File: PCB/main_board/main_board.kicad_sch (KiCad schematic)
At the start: 55 parts, among them CN1 XT30PW-M, CN2 XT30PW-M, U1 XT30PW-F, U2 W25Q32JVUUIQ, U3 W25N01GVZEIG_C907680, U4 INA226, U5 INA226, U6 RP2040, U7 AZ1117-3.3, X1 X322512MSB4SI

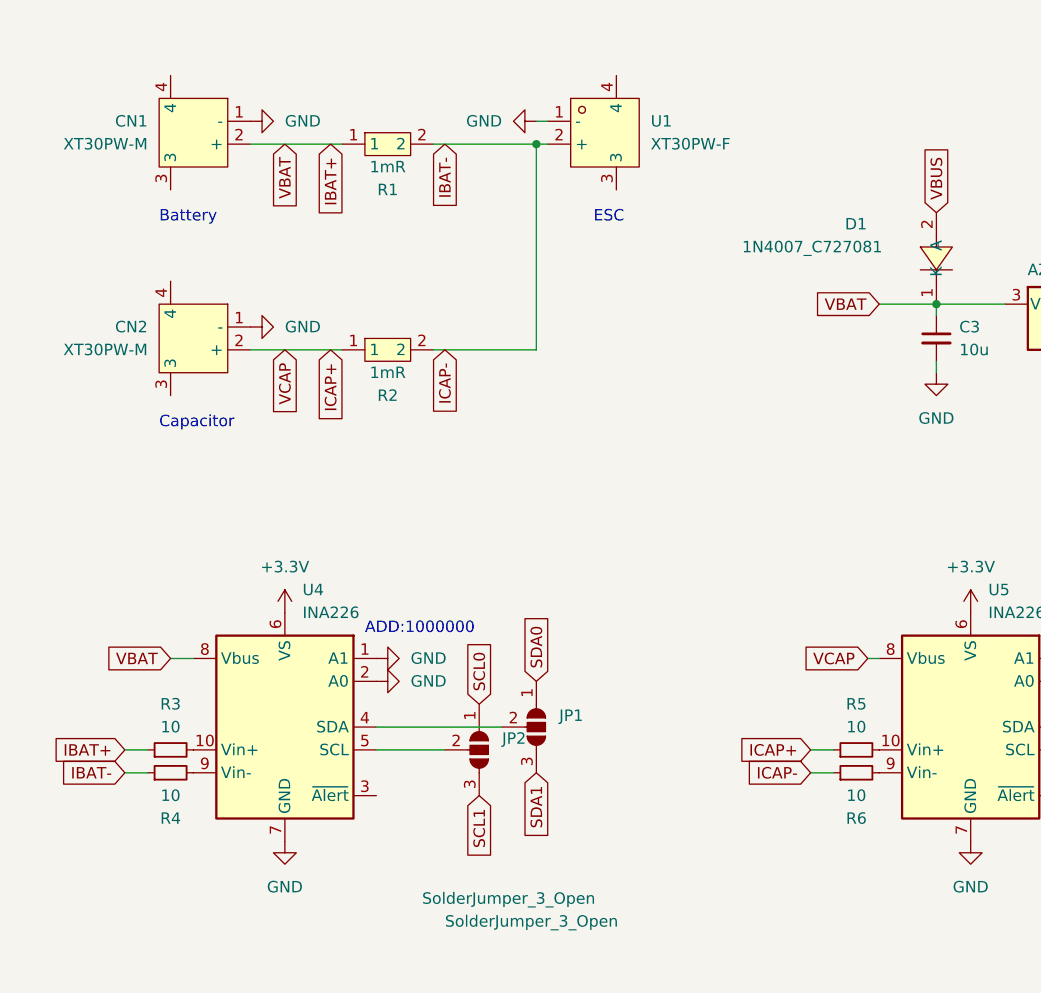
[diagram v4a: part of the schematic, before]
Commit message: Complete high current trace
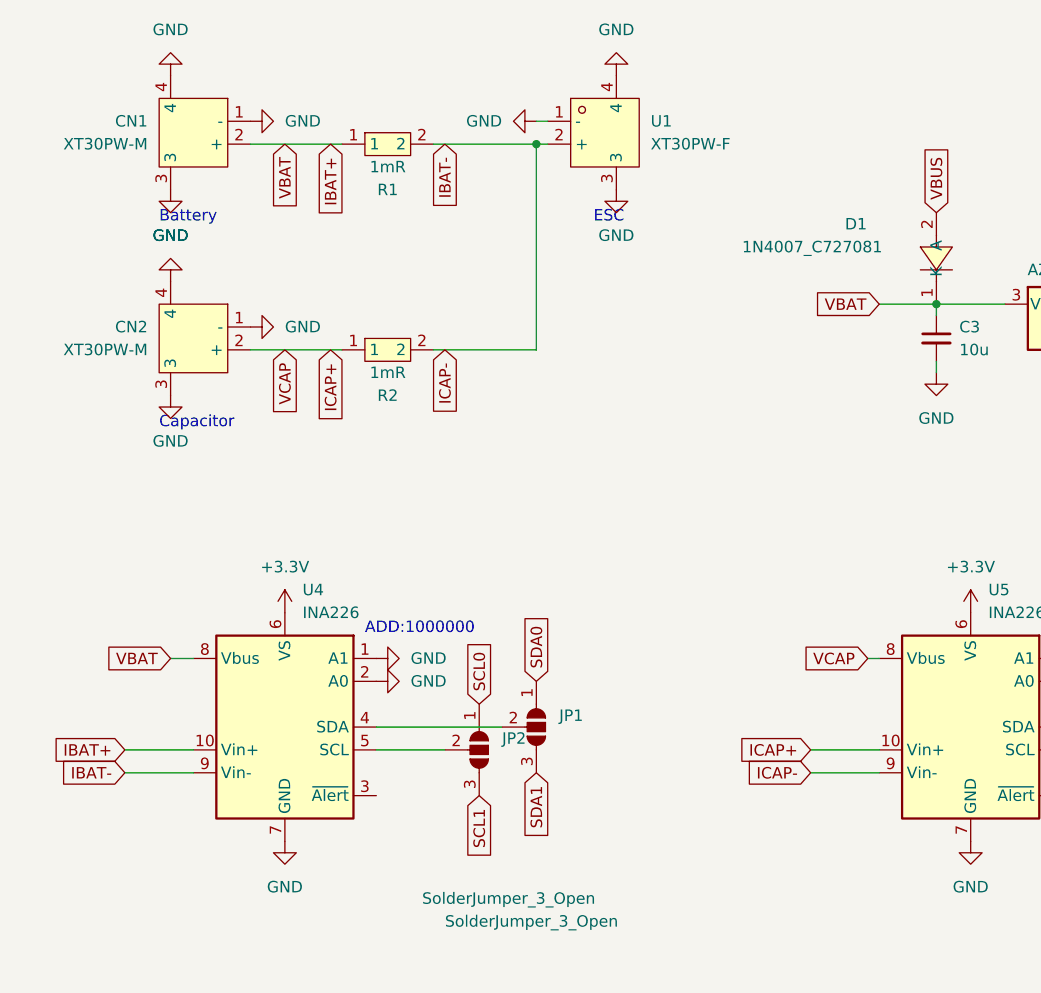
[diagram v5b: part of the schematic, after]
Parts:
- removed R3, R4, R5, R6: 10, Resistor_SMD:R_0402_1005Metric, symbol Device:R_Small
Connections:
- net GND: now also CN1.3, CN1.4, CN2.3, CN2.4, U1.3, U1.4
- net IBAT+: now also U4.10 (Vin+)
- net IBAT-: now also U4.9 (Vin-), U5.9 (Vin-)
- net ICAP+: now also U5.10 (Vin+)
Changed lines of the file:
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@@
     (stroke (width 0) (type default))
   )
-  (wire (pts (xy 123.19 110.49) (xy 125.73 110.49))
+  (wire (pts (xy 123.19 110.49) (xy 130.81 110.49))
     (stroke (width 0) (type default))
   )
@@
     (stroke (width 0) (type default))
   )
-  (wire (pts (xy 46.99 110.49) (xy 49.53 110.49))
+  (wire (pts (xy 46.99 110.49) (xy 54.61 110.49))
     (stroke (width 0) (type default))
   )
@@
     (stroke (width 0) (type default))
   )
-  (wire (pts (xy 123.19 107.95) (xy 125.73 107.95))
+  (wire (pts (xy 123.19 107.95) (xy 130.81 107.95))
     (stroke (width 0) (type default))
   )
@@
     (stroke (width 0) (type default))
   )
-  (wire (pts (xy 46.99 107.95) (xy 49.53 107.95))
+  (wire (pts (xy 46.99 107.95) (xy 54.61 107.95))
     (stroke (width 0) (type default))
   )
@@
     )
   )
+  (symbol (lib_id "power:GND") (at 52.07 68.58 0) (unit 1)
+    (in_bom yes) (on_board yes) (dnp no) (fields_autoplaced)
+    (property "Reference" "#PWR048" (at 52.07 74.93 0)
+      (effects (font (size 1.27 1.27)) hide)
+    )
+    (property "Value" "GND" (at 52.07 73.66 0)
+      (effects (font (size 1.27 1.27)))
+    )
+    (property "Footprint" "" (at 52.07 68.58 0)
+      (effects (font (size 1.27 1.27)) hide)
+    )
+    (property "Datasheet" "" (at 52.07 68.58 0)
+      (effects (font (size 1.27 1.27)) hide)
+    )
+    (pin "1")
+    (instances
+      (project "main_board"
+        (path "/fd1b5ed6-edd1-4f0a-921b-555919c14d96"
+          (reference "#PWR048") (unit 1)
+        )
+      )
+    )
+  )
   (symbol (lib_id "power:GND") (at 254 196.85 180) (unit 1)
     (in_bom yes) (on_board yes) (dnp no) (fields_autoplaced)
@@
     )
   )
-  (symbol (lib_id "Device:R_Small") (at 52.07 110.49 90) (unit 1)
-    (in_bom yes) (on_board yes) (dnp no)
-    (property "Reference" "R4" (at 52.07 115.57 90)
-      (effects (font (size 1.27 1.27)))
-    )
-    (property "Value" "10" (at 52.07 113.03 90)
-      (effects (font (size 1.27 1.27)))
-    )
-    (property "Footprint" "Resistor_SMD:R_0402_1005Metric" (at 52.07 110.49 0)
-      (effects (font (size 1.27 1.27)) hide)
-    )
-    (property "Datasheet" "~" (at 52.07 110.49 0)
-      (effects (font (size 1.27 1.27)) hide)
-    )
-    (pin "1")
-    (pin "2")
-    (instances
-      (project "main_board"
-        (path "/fd1b5ed6-edd1-4f0a-921b-555919c14d96"
-          (reference "R4") (unit 1)
+  (symbol (lib_id "power:GND") (at 101.6 45.72 0) (unit 1)
+    (in_bom yes) (on_board yes) (dnp no) (fields_autoplaced)
+    (property "Reference" "#PWR049" (at 101.6 52.07 0)
+      (effects (font (size 1.27 1.27)) hide)
+    )
+    (property "Value" "GND" (at 101.6 50.8 0)
+      (effects (font (size 1.27 1.27)))
+    )
+    (property "Footprint" "" (at 101.6 45.72 0)
+      (effects (font (size 1.27 1.27)) hide)
+    )
+    (property "Datasheet" "" (at 101.6 45.72 0)
+      (effects (font (size 1.27 1.27)) hide)
+    )
+    (pin "1")
+    (instances
+      (project "main_board"
+        (path "/fd1b5ed6-edd1-4f0a-921b-555919c14d96"
+          (reference "#PWR049") (unit 1)
+        )
+      )
+    )
+  )
+  (symbol (lib_id "power:GND") (at 52.07 45.72 0) (unit 1)
+    (in_bom yes) (on_board yes) (dnp no) (fields_autoplaced)
+    (property "Reference" "#PWR047" (at 52.07 52.07 0)
+      (effects (font (size 1.27 1.27)) hide)
+    )
+    (property "Value" "GND" (at 52.07 50.8 0)
+      (effects (font (size 1.27 1.27)))
+    )
+    (property "Footprint" "" (at 52.07 45.72 0)
+      (effects (font (size 1.27 1.27)) hide)
+    )
+    (property "Datasheet" "" (at 52.07 45.72 0)
+      (effects (font (size 1.27 1.27)) hide)
+    )
+    (pin "1")
+    (instances
+      (project "main_board"
+        (path "/fd1b5ed6-edd1-4f0a-921b-555919c14d96"
+          (reference "#PWR047") (unit 1)
         )
       )
@@
     )
   )
-  (symbol (lib_id "Device:R_Small") (at 52.07 107.95 90) (unit 1)
-    (in_bom yes) (on_board yes) (dnp no) (fields_autoplaced)
-    (property "Reference" "R3" (at 52.07 102.87 90)
-      (effects (font (size 1.27 1.27)))
-    )
-    (property "Value" "10" (at 52.07 105.41 90)
-      (effects (font (size 1.27 1.27)))
-    )
-    (property "Footprint" "Resistor_SMD:R_0402_1005Metric" (at 52.07 107.95 0)
-      (effects (font (size 1.27 1.27)) hide)
-    )
-    (property "Datasheet" "~" (at 52.07 107.95 0)
-      (effects (font (size 1.27 1.27)) hide)
-    )
-    (pin "1")
-    (pin "2")
-    (instances
-      (project "main_board"
-        (path "/fd1b5ed6-edd1-4f0a-921b-555919c14d96"
-          (reference "R3") (unit 1)
+  (symbol (lib_id "power:GND") (at 52.07 55.88 180) (unit 1)
+    (in_bom yes) (on_board yes) (dnp no) (fields_autoplaced)
+    (property "Reference" "#PWR050" (at 52.07 49.53 0)
+      (effects (font (size 1.27 1.27)) hide)
+    )
+    (property "Value" "GND" (at 52.07 50.8 0)
+      (effects (font (size 1.27 1.27)))
+    )
+    (property "Footprint" "" (at 52.07 55.88 0)
+      (effects (font (size 1.27 1.27)) hide)
+    )
+    (property "Datasheet" "" (at 52.07 55.88 0)
+      (effects (font (size 1.27 1.27)) hide)
+    )
+    (pin "1")
+    (instances
+      (project "main_board"
+        (path "/fd1b5ed6-edd1-4f0a-921b-555919c14d96"
+          (reference "#PWR050") (unit 1)
         )
       )
@@
     )
   )
-  (symbol (lib_id "Device:R_Small") (at 128.27 107.95 90) (unit 1)
-    (in_bom yes) (on_board yes) (dnp no) (fields_autoplaced)
-    (property "Reference" "R5" (at 128.27 102.87 90)
-      (effects (font (size 1.27 1.27)))
-    )
-    (property "Value" "10" (at 128.27 105.41 90)
-      (effects (font (size 1.27 1.27)))
-    )
-    (property "Footprint" "Resistor_SMD:R_0402_1005Metric" (at 128.27 107.95 0)
-      (effects (font (size 1.27 1.27)) hide)
-    )
-    (property "Datasheet" "~" (at 128.27 107.95 0)
-      (effects (font (size 1.27 1.27)) hide)
-    )
-    (pin "1")
-    (pin "2")
-    (instances
-      (project "main_board"
-        (path "/fd1b5ed6-edd1-4f0a-921b-555919c14d96"
-          (reference "R5") (unit 1)
-        )
-      )
-    )
-  )
   (symbol (lib_id "Sensor_Energy:INA226") (at 64.77 105.41 0) (unit 1)
     (in_bom yes) (on_board yes) (dnp no) (fields_autoplaced)
@@
     )
   )
-  (symbol (lib_id "Device:R_Small") (at 128.27 110.49 90) (unit 1)
-    (in_bom yes) (on_board yes) (dnp no)
-    (property "Reference" "R6" (at 128.27 115.57 90)
-      (effects (font (size 1.27 1.27)))
-    )
-    (property "Value" "10" (at 128.27 113.03 90)
-      (effects (font (size 1.27 1.27)))
-    )
-    (property "Footprint" "Resistor_SMD:R_0402_1005Metric" (at 128.27 110.49 0)
-      (effects (font (size 1.27 1.27)) hide)
-    )
-    (property "Datasheet" "~" (at 128.27 110.49 0)
-      (effects (font (size 1.27 1.27)) hide)
-    )
-    (pin "1")
-    (pin "2")
-    (instances
-      (project "main_board"
-        (path "/fd1b5ed6-edd1-4f0a-921b-555919c14d96"
-          (reference "R6") (unit 1)
-        )
-      )
-    )
-  )
   (symbol (lib_id "power:+3.3V") (at 207.01 180.34 90) (unit 1)
     (in_bom yes) (on_board yes) (dnp no) (fields_autoplaced)
@@
     )
   )
+  (symbol (lib_id "power:GND") (at 52.07 33.02 180) (unit 1)
+    (in_bom yes) (on_board yes) (dnp no) (fields_autoplaced)
+    (property "Reference" "#PWR051" (at 52.07 26.67 0)
+      (effects (font (size 1.27 1.27)) hide)
+    )
+    (property "Value" "GND" (at 52.07 27.94 0)
+      (effects (font (size 1.27 1.27)))
+    )
+    (property "Footprint" "" (at 52.07 33.02 0)
+      (effects (font (size 1.27 1.27)) hide)
+    )
+    (property "Datasheet" "" (at 52.07 33.02 0)
+      (effects (font (size 1.27 1.27)) hide)
+    )
+    (pin "1")
+    (instances
+      (project "main_board"
+        (path "/fd1b5ed6-edd1-4f0a-921b-555919c14d96"
+          (reference "#PWR051") (unit 1)
+        )
+      )
+    )
+  )
   (symbol (lib_id "Device:C_Small") (at 128.27 161.29 90) (unit 1)
     (in_bom yes) (on_board yes) (dnp no)
@@
         )
       )
+    )
+  )
+  (symbol (lib_id "power:GND") (at 101.6 33.02 180) (unit 1)
+    (in_bom yes) (on_board yes) (dnp no) (fields_autoplaced)
+    (property "Reference" "#PWR052" (at 101.6 26.67 0)
+      (effects (font (size 1.27 1.27)) hide)
+    )
+    (property "Value" "GND" (at 101.6 27.94 0)
+      (effects (font (size 1.27 1.27)))
+    )
+    (property "Footprint" "" (at 101.6 33.02 0)
+      (effects (font (size 1.27 1.27)) hide)
+    )
+    (property "Datasheet" "" (at 101.6 33.02 0)
+      (effects (font (size 1.27 1.27)) hide)
+    )
+    (pin "1")
+    (instances
+      (project "main_board"
+        (path "/fd1b5ed6-edd1-4f0a-921b-555919c14d96"
+          (reference "#PWR052") (unit 1)
+        )
+      )

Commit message: Complete USB DP routing
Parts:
- added TP1: SWCLK, TestPoint:TestPoint_Pad_1.5x1.5mm, symbol Connector:TestPoint
- added TP2: SWD, TestPoint:TestPoint_Pad_1.5x1.5mm, symbol Connector:TestPoint
- added TP3: UART0 TX, TestPoint:TestPoint_Pad_1.5x1.5mm, symbol Connector:TestPoint
- added TP4: UART0 RX, TestPoint:TestPoint_Pad_1.5x1.5mm, symbol Connector:TestPoint
- added TP5, TP6: GND, TestPoint:TestPoint_Pad_1.5x1.5mm, symbol Connector:TestPoint
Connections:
- net GND: now also Card1.10 (EP), Card1.11 (EP), Card1.12 (EP), Card1.13 (EP), U3.9 (EP), USB1.13 (SHELL), USB1.14 (SHELL), TP5.1, TP6.1
- net USB+: now reaches R17.1, USB1.7 (DN1)
- net USB-: now reaches R16.1, USB1.6 (DP1)
- net at U6.24 (SWCLK): now also TP1.1
- net at U6.25 (SWD): now also TP2.1
- net TX0: now reaches U6.28 (GPIO17)
- net TX0: now also TP3.1
- net RX0: now reaches U6.29 (GPIO18)
- net RX0: now also TP4.1

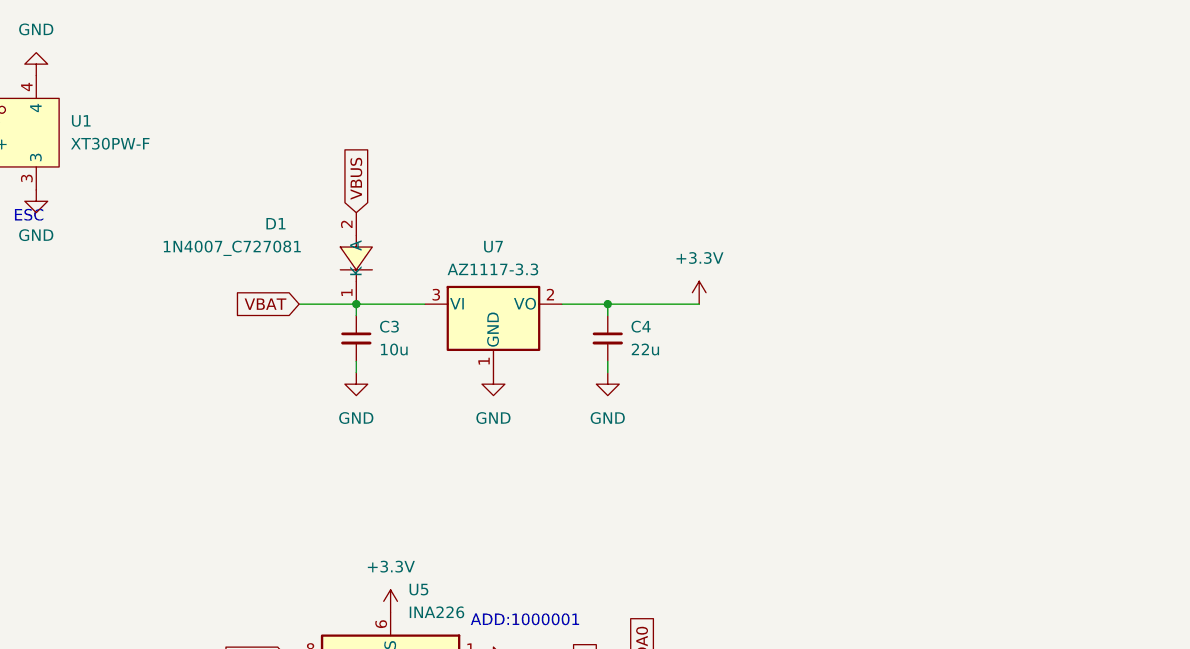
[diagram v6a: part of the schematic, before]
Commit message: Change LDO to BUCK converter
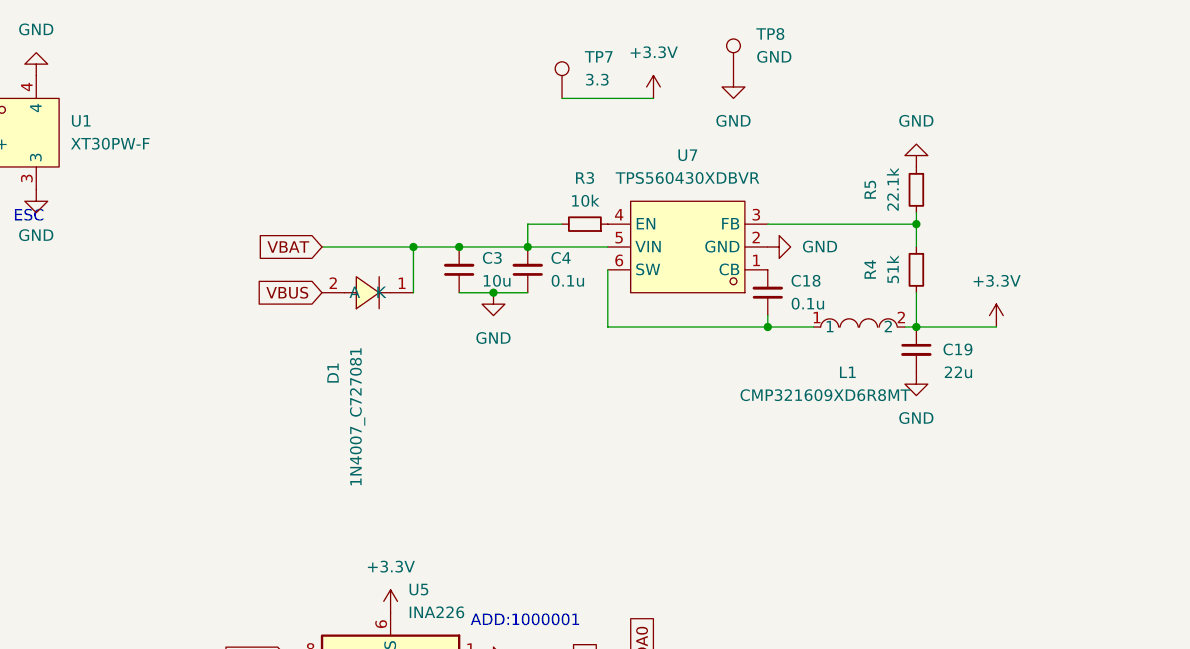
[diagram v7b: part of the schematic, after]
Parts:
- removed U7: AZ1117-3.3, Package_TO_SOT_SMD:SOT-89-3, symbol Regulator_Linear:AZ1117-3.3
- added C18: 0.1u, Capacitor_SMD:C_0402_1005Metric, symbol Device:C_Small
- added C19: 22u, Capacitor_SMD:C_0805_2012Metric, symbol Device:C_Small
- added L1: CMP321609XD6R8MT, pcb_lib:L1206, symbol pcb_lib:CMP321609XD6R8MT
- added R3: 10k, Capacitor_SMD:C_0402_1005Metric, symbol Device:R_Small
- added R4: 51k, Capacitor_SMD:C_0402_1005Metric, symbol Device:R_Small
- added R5: 22.1k, Capacitor_SMD:C_0402_1005Metric, symbol Device:R_Small
- added TP7: 3.3, TestPoint:TestPoint_Pad_1.5x1.5mm, symbol Connector:TestPoint
- added TP8: GND, TestPoint:TestPoint_Pad_1.5x1.5mm, symbol Connector:TestPoint
- added U7: TPS560430XDBVR, pcb_lib:SOT-23-6_L2.9-W1.6-P0.95-LS2.8-BL, symbol pcb_lib:TPS560430XDBVR
- C4: value 22u -> 0.1u
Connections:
- net +3.3V: now also C19.1, L1.2, R4.2, TP7.1; no longer C4.1
- net GND: now also C3.1, C4.1, C19.2, R5.1, TP8.1, U7.2 (GND); no longer C3.2, C4.2
- net IBAT+: now also C3.2, C4.2, R3.2, U7.5 (VIN); no longer C3.1
- new net: R4.1, R5.2, U7.3 (FB)
- new net: C18.1, L1.1, U7.6 (SW)
- new net: C18.2, U7.1 (CB)
- new net: R3.1, U7.4 (EN)
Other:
- moved on the sheet: D1

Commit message: Change INA226 package for SMT
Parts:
- C3, C4: footprint Capacitor_SMD:C_0402_1005Metric -> Capacitor_SMD:C_0603_1608Metric
- U4, U5: footprint Package_SO:VSSOP-10_3x3mm_P0.5mm -> pcb_lib:MSOP-10_L3.0-W3.0-P0.50-LS5.0-BL
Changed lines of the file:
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@@
       (effects (font (size 1.27 1.27)) (justify left))
     )
-    (property "Footprint" "Package_SO:VSSOP-10_3x3mm_P0.5mm" (at 161.29 116.84 0)
+    (property "Footprint" "pcb_lib:MSOP-10_L3.0-W3.0-P0.50-LS5.0-BL" (at 161.29 116.84 0)
       (effects (font (size 1.27 1.27)) hide)
     )
@@
       (effects (font (size 1.27 1.27)) (justify left))
     )
-    (property "Footprint" "Package_SO:VSSOP-10_3x3mm_P0.5mm" (at 85.09 116.84 0)
+    (property "Footprint" "pcb_lib:MSOP-10_L3.0-W3.0-P0.50-LS5.0-BL" (at 85.09 116.84 0)
       (effects (font (size 1.27 1.27)) hide)
     )
@@
       (effects (font (size 1.27 1.27)) (justify right))
     )
-    (property "Footprint" "Capacitor_SMD:C_0402_1005Metric" (at 148.59 54.61 0)
+    (property "Footprint" "Capacitor_SMD:C_0603_1608Metric" (at 148.59 54.61 0)
       (effects (font (size 1.27 1.27)) hide)
     )
@@
       (effects (font (size 1.27 1.27)) (justify right))
     )
-    (property "Footprint" "Capacitor_SMD:C_0402_1005Metric" (at 156.21 54.61 0)
-      (effects (font (size 1.27 1.27)) hide)
-    )
+    (property "Footprint" "Capacitor_SMD:C_0603_1608Metric" (at 156.21 54.61 0)
+      (effects (font (size 1.27 1.27)) hide)
+    )
